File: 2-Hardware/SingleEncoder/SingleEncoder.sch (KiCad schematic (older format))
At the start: 23 parts, among them J1 PMOD_SINGLE, P1 CONN_01X06, P2 CONN_01X04, U1 TPS60131

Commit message: Associated footprints, reimported to board. Layout not done.
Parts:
- AT1: footprint (none) -> SMD:SSOP_08_3.0mm_2.0mm_0.5mm
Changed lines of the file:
@@
 LIBS:LogicDevices
 LIBS:SingleEncoder-cache
-EELAYER 25 0
+EELAYER 26 0
 EELAYER END
 $Descr A4 11693 8268
@@
 F 0 "AT1" H 10900 1800 60  0000 C CNN
 F 1 "TXB0102" H 10900 1200 60  0000 C CNN
-F 2 "" H 11150 1450 60  0001 C CNN
+F 2 "SMD:SSOP_08_3.0mm_2.0mm_0.5mm" H 11150 1450 60  0001 C CNN
 F 3 "" H 11150 1450 60  0000 C CNN
 F 4 "296-22862-1-ND" H 10900 1500 60  0001 C CNN "DigikeyNumber"
@@
 F 0 "AT1" H 8650 2200 60  0000 C CNN
 F 1 "TXB0102" H 8650 2400 60  0000 C CNN
-F 2 "" H 8900 2250 60  0001 C CNN
+F 2 "SMD:SSOP_08_3.0mm_2.0mm_0.5mm" H 8900 2250 60  0001 C CNN
 F 3 "" H 8900 2250 60  0000 C CNN
 	1    8650 2300
@@
 F 0 "AT1" H 8650 3100 60  0000 C CNN
 F 1 "TXB0102" H 8650 3300 60  0000 C CNN
-F 2 "" H 8900 3150 60  0001 C CNN
+F 2 "SMD:SSOP_08_3.0mm_2.0mm_0.5mm" H 8900 3150 60  0001 C CNN
 F 3 "" H 8900 3150 60  0000 C CNN
 	2    8650 3200

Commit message: Updated board layout to use level shifter
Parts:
- C7, C8: value CAP -> 0.1uF
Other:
- moved on the sheet: AT1A, AT1C, C7
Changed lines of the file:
@@
 LIBS:LogicDevices
 LIBS:SingleEncoder-cache
-EELAYER 26 0
+EELAYER 25 0
 EELAYER END
 $Descr A4 11693 8268
@@
 Title "Quadrature Encoder PMOD-Compatible Interface"
 Date ""
-Rev "A"
+Rev "B"
 Comp ""
 Comment1 "Drawn by: Ian McInerney"
@@
 Text Label 1450 1850 0    60   ~ 0
 LOGIC_A
-Text Label 1450 1950 0    60   ~ 0
+Text Label 1450 2150 0    60   ~ 0
 LOGIC_B
 Wire Wire Line
 	1450 1850 1350 1850
-Wire Wire Line
-	1350 1950 1450 1950
 Wire Wire Line
 	1450 2050 1350 2050
@@
 Wire Wire Line
 	1000 4200 1000 4250
-NoConn ~ 1350 2150
+NoConn ~ 1350 1950
 NoConn ~ 3750 1350
 Wire Wire Line
@@
 L GND #PWR012
 U 1 1 55A5A23B
-P 10500 1750
-F 0 "#PWR012" H 10500 1500 50  0001 C CNN
-F 1 "GND" H 10500 1600 50  0000 C CNN
-F 2 "" H 10500 1750 60  0000 C CNN
-F 3 "" H 10500 1750 60  0000 C CNN
-	1    10500 1750
+P 10400 1700
+F 0 "#PWR012" H 10400 1450 50  0001 C CNN
+F 1 "GND" H 10400 1550 50  0000 C CNN
+F 2 "" H 10400 1700 60  0000 C CNN
+F 3 "" H 10400 1700 60  0000 C CNN
+	1    10400 1700
 	1    0    0    -1
 $EndComp
@@
 L TXB0102 AT1
 U 3 1 58852CDD
+P 8650 2300
+F 0 "AT1" H 8650 2400 60  0000 C CNN
+F 1 "TXB0102" H 8650 2200 60  0000 C CNN
+F 2 "SMD:SSOP_08_3.0mm_2.0mm_0.5mm" H 8900 2250 60  0001 C CNN
+F 3 "" H 8900 2250 60  0000 C CNN
+F 4 "296-22862-1-ND" H 8650 2300 60  0001 C CNN "DigikeyNumber"
+F 5 "Texas Instruments" H 8650 2300 60  0001 C CNN "Manufacturer"
+F 6 "TXB0102" H 8650 2300 60  0001 C CNN "ManufacturerNumber"
+	3    8650 2300
+	-1   0    0    1
+$EndComp
+$Comp
+L TXB0102 AT1
+U 1 1 58852D88
 P 10900 1500
-F 0 "AT1" H 10900 1800 60  0000 C CNN
-F 1 "TXB0102" H 10900 1200 60  0000 C CNN
+F 0 "AT1" H 10900 1200 60  0000 C CNN
+F 1 "TXB0102" H 10900 1800 60  0000 C CNN
 F 2 "SMD:SSOP_08_3.0mm_2.0mm_0.5mm" H 11150 1450 60  0001 C CNN
 F 3 "" H 11150 1450 60  0000 C CNN
-F 4 "296-22862-1-ND" H 10900 1500 60  0001 C CNN "DigikeyNumber"
-F 5 "Texas Instruments" H 10900 1500 60  0001 C CNN "Manufacturer"
-F 6 "TXB0102" H 10900 1500 60  0001 C CNN "ManufacturerNumber"
-	3    10900 1500
-	1    0    0    -1
-$EndComp
-$Comp
-L TXB0102 AT1
-U 1 1 58852D88
-P 8650 2300
-F 0 "AT1" H 8650 2200 60  0000 C CNN
-F 1 "TXB0102" H 8650 2400 60  0000 C CNN
-F 2 "SMD:SSOP_08_3.0mm_2.0mm_0.5mm" H 8900 2250 60  0001 C CNN
-F 3 "" H 8900 2250 60  0000 C CNN
-	1    8650 2300
-	-1   0    0    1
+	1    10900 1500
+	1    0    0    -1
 $EndComp
 $Comp
@@
 	10300 1450 10650 1450
 Wire Wire Line
-	10500 1650 10500 1750
-Wire Wire Line
-	9750 1650 10650 1650
-Text Label 10450 1550 2    60   ~ 0
+	9700 1650 10650 1650
+Text Label 10350 1550 2    60   ~ 0
 EN
-Wire Wire Line
-	10450 1550 10650 1550
 $Comp
 L CAP C7
 U 1 1 58854AD5
-P 9750 1400
-F 0 "C7" H 9750 1470 60  0000 R CNN
-F 1 "CAP" H 9750 1320 60  0000 R CNN
-F 2 "SMD:SMD_0805" V 9490 1300 60  0001 C CNN
-F 3 "" V 9590 1400 60  0001 C CNN
-	1    9750 1400
+P 9700 1400
+F 0 "C7" H 9700 1470 60  0000 R CNN
+F 1 "0.1uF" H 9700 1320 60  0000 R CNN
+F 2 "SMD:SMD_0805" V 9440 1300 60  0001 C CNN
+F 3 "" V 9540 1400 60  0001 C CNN
+	1    9700 1400
 	1    0    0    -1
 $EndComp
@@
 P 10050 1400
 F 0 "C8" H 10050 1470 60  0000 R CNN
-F 1 "CAP" H 10050 1320 60  0000 R CNN
+F 1 "0.1uF" H 10050 1320 60  0000 R CNN
 F 2 "SMD:SMD_0805" V 9790 1300 60  0001 C CNN
 F 3 "" V 9890 1400 60  0001 C CNN
@@
 $EndComp
 Wire Wire Line
-	8400 2300 7950 2300
+	7950 2300 8400 2300
 Wire Wire Line
 	10050 1200 10050 1150
 Wire Wire Line
-	10050 1600 10050 1650
-Connection ~ 10500 1650
-Wire Wire Line
-	9750 1600 9750 1650
+	10050 1650 10050 1600
+Wire Wire Line
+	9700 1600 9700 1650
 Connection ~ 10050 1650
 Wire Wire Line
-	9750 900  9750 1200
+	9700 900  9700 1200
 Wire Wire Line
 	10050 1150 10300 1150
 Connection ~ 10300 1150
 Wire Wire Line
-	9750 900  10500 900
+	9700 900  10500 900
 Connection ~ 10500 900
 $Comp
@@
 	1    0    0    -1
 $EndComp
+Wire Wire Line
+	10350 1550 10650 1550
+Wire Wire Line
+	10400 1650 10400 1700
+Connection ~ 10400 1650
+Wire Wire Line
+	1450 2150 1350 2150
 $EndSCHEMATC

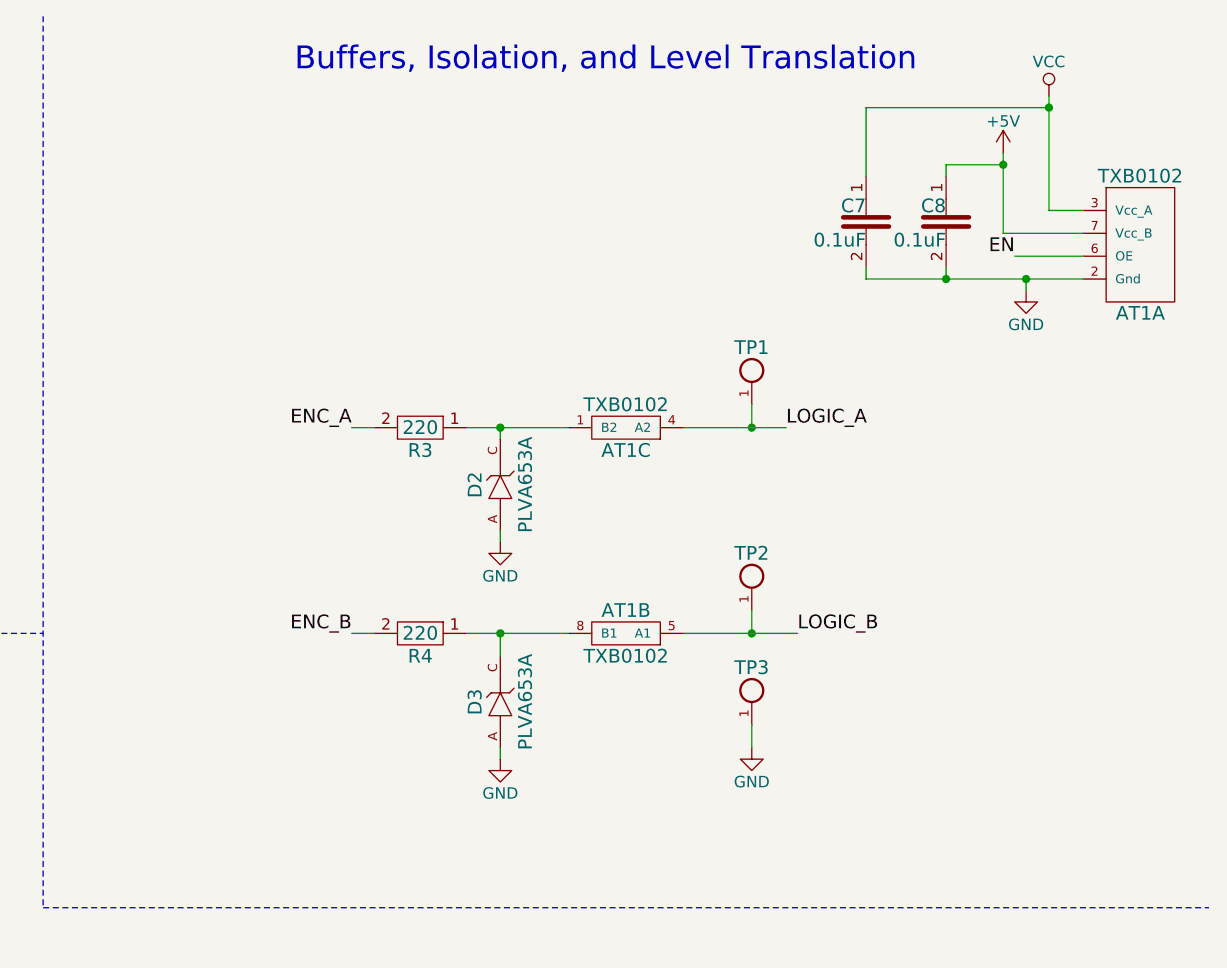
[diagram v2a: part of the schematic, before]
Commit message: Updated isolation circuit
- Swapped TXB0102 for 2 TXB0101
- Re-did board layout to accomodate new parts
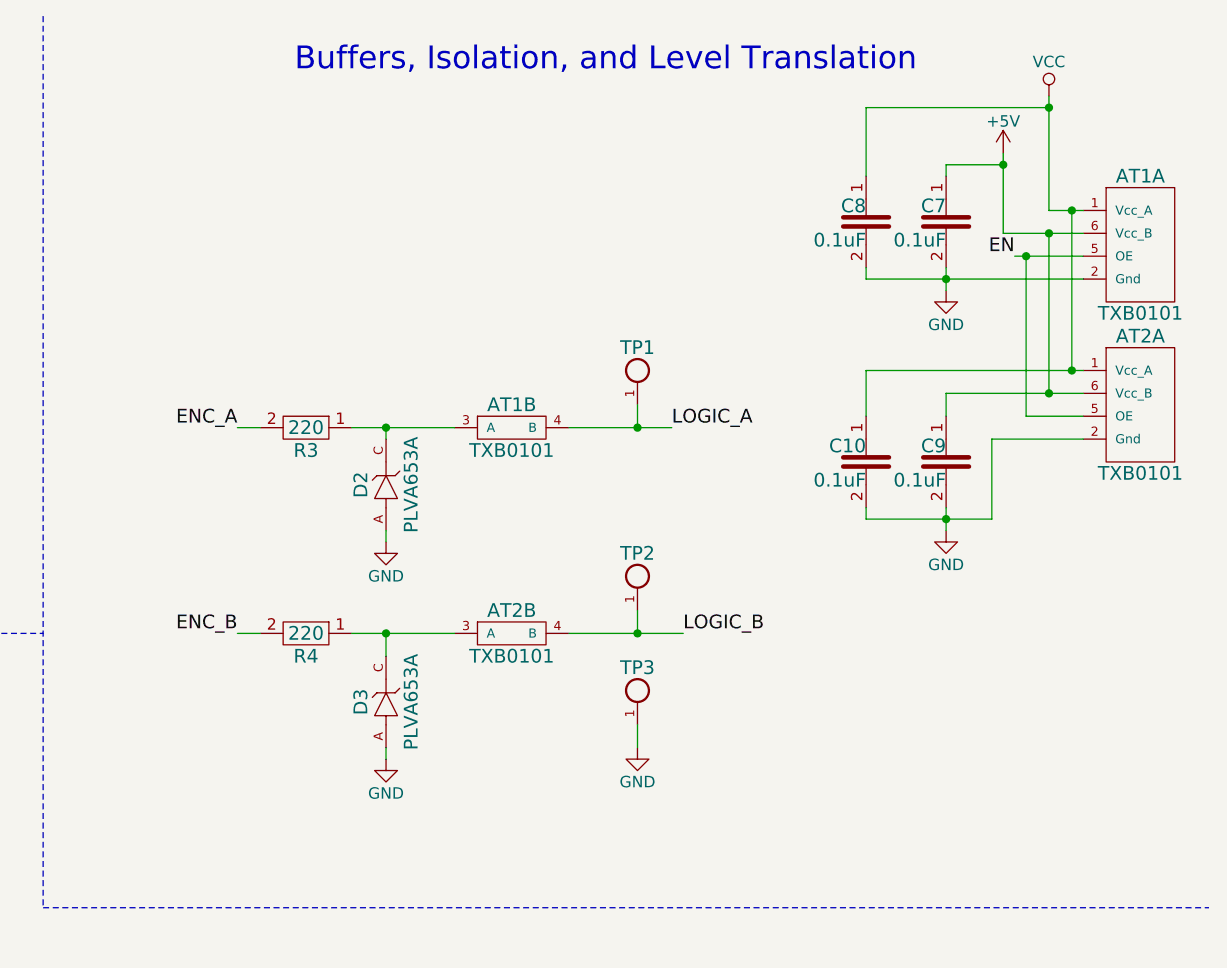
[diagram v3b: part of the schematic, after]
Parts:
- removed AT1: TXB0102, SMD:SSOP_08_3.0mm_2.0mm_0.5mm, symbol TXB0102
- added AT1, AT2: TXB0101, SMD:SOT-23-6, symbol TXB0101
- added C10, C8: 0.1uF, SMD:SMD_0805, symbol CAP
- C7: DigikeyNumber (none) -> 311-1141-1-ND; Manufacturer (none) -> Yageo; ManufacturerNumber (none) -> CC0805KRX7R8BB104
- C9: renamed from C8; DigikeyNumber (none) -> 311-1141-1-ND; Manufacturer (none) -> Yageo; ManufacturerNumber (none) -> CC0805KRX7R8BB104
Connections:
- net +5V: now also C7.1, AT1.6 (Vcc_B), AT2.6 (Vcc_B)
- net EN: now also AT1.5 (OE), AT2.5 (OE)
- net GND: now also AT1.2 (Gnd), AT2.2 (Gnd), C10.2, C8.2
- net LOGIC_A: now also AT1.4 (B)
- net LOGIC_B: now also AT2.4 (B)
- net VCC: now also AT1.1 (Vcc_A), AT2.1 (Vcc_A), C10.1, C8.1; no longer C7.1
- net at D2.C, R3.1: now also AT1.3 (A)
- net at D3.C, R4.1: now also AT2.3 (A)
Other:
- moved on the sheet: C7, C9, D2, D3, R3, R4, TP1, TP2, TP3

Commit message: Revised layout and created BOM
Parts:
- AT1, AT2: DigikeyNumber (none) -> 296-21664-1-ND; Manufacturer (none) -> Texas Instruments; ManufacturerNumber (none) -> TXB0101DBVR
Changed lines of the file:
@@
 F 2 "SMD:SOT-23-6" H 11150 2150 60  0001 C CNN
 F 3 "" H 11150 2150 60  0000 C CNN
+F 4 "296-21664-1-ND" H 10900 2200 60  0001 C CNN "DigikeyNumber"
+F 5 "Texas Instruments" H 10900 2200 60  0001 C CNN "Manufacturer"
+F 6 "TXB0101DBVR" H 10900 2200 60  0001 C CNN "ManufacturerNumber"
 	1    10900 2200
 	1    0    0    -1
@@
 F 2 "SMD:SOT-23-6" H 11150 1450 60  0001 C CNN
 F 3 "" H 11150 1450 60  0000 C CNN
+F 4 "296-21664-1-ND" H 10900 1500 60  0001 C CNN "DigikeyNumber"
+F 5 "Texas Instruments" H 10900 1500 60  0001 C CNN "Manufacturer"
+F 6 "TXB0101DBVR" H 10900 1500 60  0001 C CNN "ManufacturerNumber"
 	1    10900 1500
 	1    0    0    -1
@@
 F 2 "SMD:SOT-23-6" H 8400 2250 60  0001 C CNN
 F 3 "" H 8400 2250 60  0000 C CNN
+F 4 "296-21664-1-ND" H 8150 2300 60  0001 C CNN "DigikeyNumber"
+F 5 "Texas Instruments" H 8150 2300 60  0001 C CNN "Manufacturer"
+F 6 "TXB0101DBVR" H 8150 2300 60  0001 C CNN "ManufacturerNumber"
 	2    8150 2300
 	1    0    0    -1
@@
 F 2 "SMD:SOT-23-6" H 8400 3150 60  0001 C CNN
 F 3 "" H 8400 3150 60  0000 C CNN
+F 4 "296-21664-1-ND" H 8150 3200 60  0001 C CNN "DigikeyNumber"
+F 5 "Texas Instruments" H 8150 3200 60  0001 C CNN "Manufacturer"
+F 6 "TXB0101DBVR" H 8150 3200 60  0001 C CNN "ManufacturerNumber"
 	2    8150 3200
 	1    0    0    -1
@@
 	10050 2650 10050 2750
 $Comp
-L GND #PWR?
+L GND #PWR021
 U 1 1 59DC11A3
 P 10050 2750
-F 0 "#PWR?" H 10050 2500 50  0001 C CNN
+F 0 "#PWR021" H 10050 2500 50  0001 C CNN
 F 1 "GND" H 10050 2600 50  0000 C CNN
 F 2 "" H 10050 2750 60  0000 C CNN

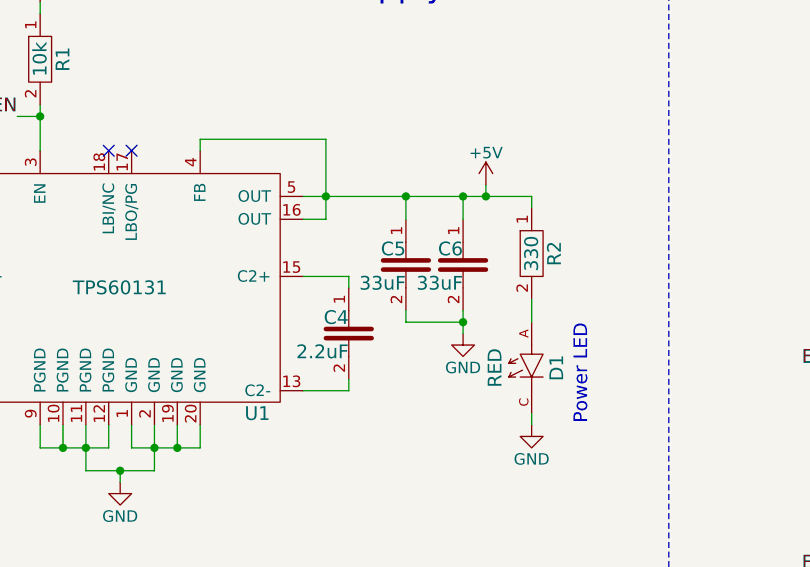
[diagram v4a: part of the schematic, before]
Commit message: Update BOM to make sure all parts are in stock.
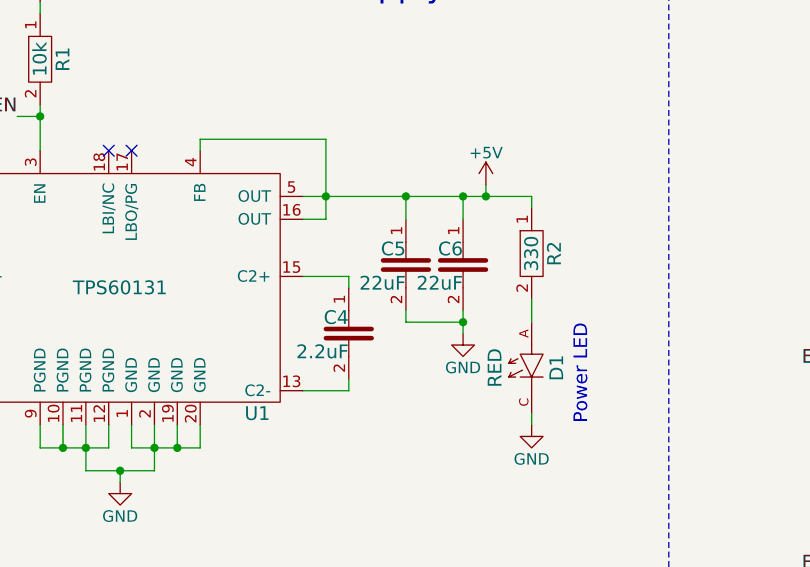
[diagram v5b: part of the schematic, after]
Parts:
- C3, C4: DigikeyNumber 445-1588-1-ND -> 311-3425-1-ND; Manufacturer TDK Corporation -> Yageo; ManufacturerNumber C2012X5R1A225K085AA -> CC0805KRX5R6BB225
- C5, C6: value 33uF -> 22uF; DigikeyNumber 445-8238-1-ND -> 1276-6786-1-ND; Manufacturer TDK Corporation -> Samsung Electro-Mechanics America, Inc.; ManufacturerNumber C2012X5R1A336M125AC -> CL21A226KPCLRNC
- R1: DigikeyNumber P10.0KCCT-ND -> RMCF0805FT10K0CT-ND; Manufacturer Panasonic Electronic Components -> Stackpole Electronics Inc; ManufacturerNumber ERJ-6ENF1002V -> RMCF0805FT10K0
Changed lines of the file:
@@
 F 2 "SMD:SMD_0805" V 3090 850 60  0001 C CNN
 F 3 "" V 3190 950 60  0001 C CNN
-F 4 "P10.0KCCT-ND" H 3350 950 60  0001 C CNN "DigikeyNumber"
-F 5 "Panasonic Electronic Components" H 3350 950 60  0001 C CNN "Manufacturer"
-F 6 "ERJ-6ENF1002V" H 3350 950 60  0001 C CNN "ManufacturerNumber"
+F 4 "RMCF0805FT10K0CT-ND" H 3350 950 60  0001 C CNN "DigikeyNumber"
+F 5 "Stackpole Electronics Inc" H 3350 950 60  0001 C CNN "Manufacturer"
+F 6 "RMCF0805FT10K0" H 3350 950 60  0001 C CNN "ManufacturerNumber"
 	1    3350 950
 	1    0    0    -1
@@
 F 2 "SMD:SMD_0805" V 2540 2050 60  0001 C CNN
 F 3 "" V 2640 2150 60  0001 C CNN
-F 4 "445-1588-1-ND" H 2800 2150 60  0001 C CNN "DigikeyNumber"
-F 5 "TDK Corporation" H 2800 2150 60  0001 C CNN "Manufacturer"
-F 6 "C2012X5R1A225K085AA" H 2800 2150 60  0001 C CNN "ManufacturerNumber"
+F 4 "311-3425-1-ND" H 2800 2150 60  0001 C CNN "DigikeyNumber"
+F 5 "Yageo" H 2800 2150 60  0001 C CNN "Manufacturer"
+F 6 "CC0805KRX5R6BB225" H 2800 2150 60  0001 C CNN "ManufacturerNumber"
 	1    2800 2150
 	1    0    0    -1
@@
 F 2 "SMD:SMD_0805" V 4440 2050 60  0001 C CNN
 F 3 "" V 4540 2150 60  0001 C CNN
-F 4 "445-1588-1-ND" H 4700 2150 60  0001 C CNN "DigikeyNumber"
-F 5 "TDK Corporation" H 4700 2150 60  0001 C CNN "Manufacturer"
-F 6 "C2012X5R1A225K085AA" H 4700 2150 60  0001 C CNN "ManufacturerNumber"
+F 4 "311-3425-1-ND" H 4700 2150 60  0001 C CNN "DigikeyNumber"
+F 5 "Yageo" H 4700 2150 60  0001 C CNN "Manufacturer"
+F 6 "CC0805KRX5R6BB225" H 4700 2150 60  0001 C CNN "ManufacturerNumber"
 	1    4700 2150
 	1    0    0    -1
@@
 P 5200 1850
 F 0 "C6" H 5200 1920 60  0000 R CNN
-F 1 "33uF" H 5200 1770 60  0000 R CNN
+F 1 "22uF" H 5200 1770 60  0000 R CNN
 F 2 "SMD:SMD_0805" V 4940 1750 60  0001 C CNN
 F 3 "" V 5040 1850 60  0001 C CNN
-F 4 "445-8238-1-ND" H 5200 1850 60  0001 C CNN "DigikeyNumber"
-F 5 "TDK Corporation" H 5200 1850 60  0001 C CNN "Manufacturer"
-F 6 "C2012X5R1A336M125AC" H 5200 1850 60  0001 C CNN "ManufacturerNumber"
+F 4 "1276-6786-1-ND" H 5200 1850 60  0001 C CNN "DigikeyNumber"
+F 5 "Samsung Electro-Mechanics America, Inc." H 5200 1850 60  0001 C CNN "Manufacturer"
+F 6 "CL21A226KPCLRNC" H 5200 1850 60  0001 C CNN "ManufacturerNumber"
 	1    5200 1850
 	1    0    0    -1
@@
 P 4950 1850
 F 0 "C5" H 4950 1920 60  0000 R CNN
-F 1 "33uF" H 4950 1770 60  0000 R CNN
+F 1 "22uF" H 4950 1770 60  0000 R CNN
 F 2 "SMD:SMD_0805" V 4690 1750 60  0001 C CNN
 F 3 "" V 4790 1850 60  0001 C CNN
-F 4 "445-8238-1-ND" H 4950 1850 60  0001 C CNN "DigikeyNumber"
-F 5 "TDK Corporation" H 4950 1850 60  0001 C CNN "Manufacturer"
-F 6 "C2012X5R1A336M125AC" H 4950 1850 60  0001 C CNN "ManufacturerNumber"
+F 4 "1276-6786-1-ND" H 4950 1850 60  0001 C CNN "DigikeyNumber"
+F 5 "Samsung Electro-Mechanics America, Inc." H 4950 1850 60  0001 C CNN "Manufacturer"
+F 6 "CL21A226KPCLRNC" H 4950 1850 60  0001 C CNN "ManufacturerNumber"
 	1    4950 1850
 	1    0    0    -1
